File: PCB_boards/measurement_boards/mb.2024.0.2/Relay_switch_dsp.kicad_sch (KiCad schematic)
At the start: 8 parts, among them K1 G5LE-1, K2 G5LE-1, Q1 ZVN4206ASTZ, Q2 ZVN4206ASTZ

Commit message: update measurement board
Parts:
- Q1, Q2: symbol ZVN4206ASTZ:ZVN4206ASTZ -> ZVN4206A:ZVN4206ASTZ; Manufacturer_Name Diodes Incorporated -> Diodes Inc.
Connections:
- net out_12v_DPS renamed out_12v_DSP
- net out_GND_DPS renamed out_GND_DSP

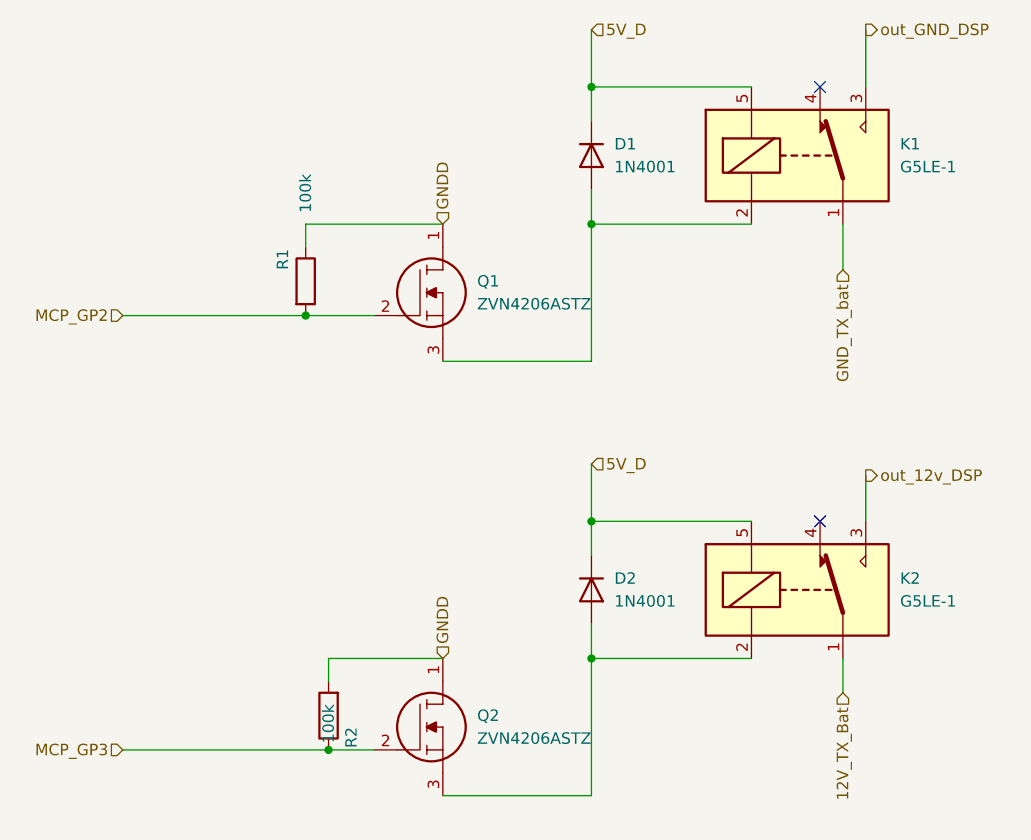
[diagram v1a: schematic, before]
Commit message: update diode 1n4007
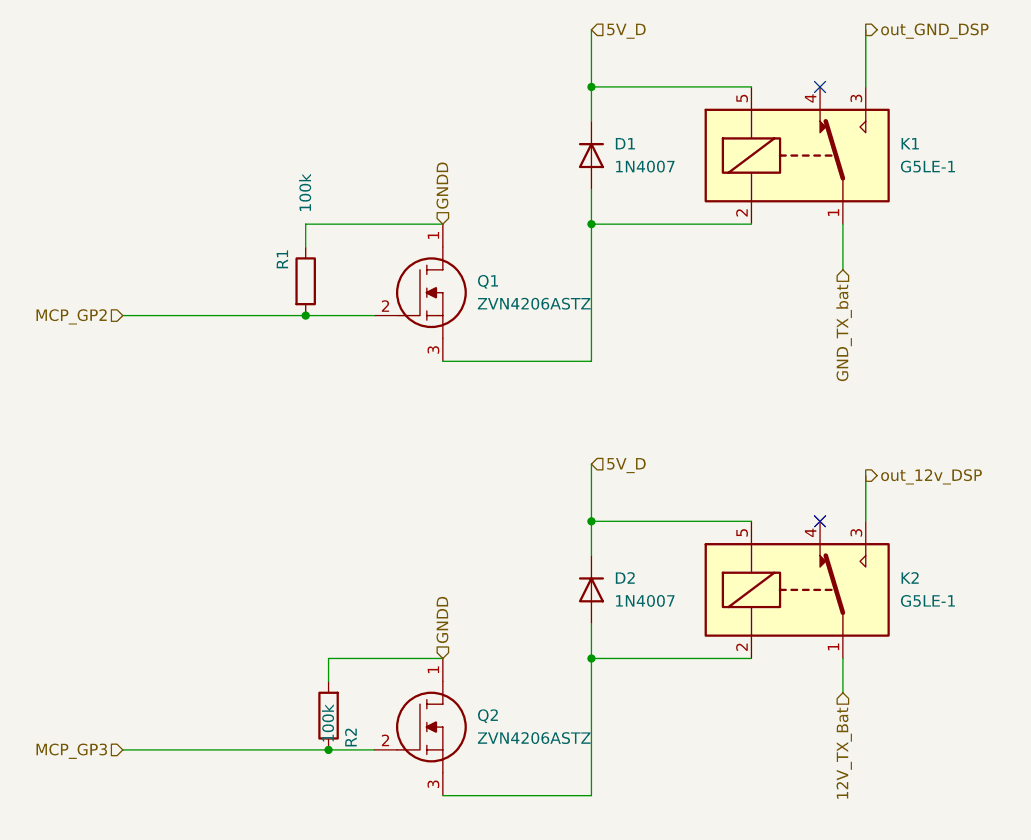
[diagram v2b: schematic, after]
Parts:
- D1, D2: value 1N4001 -> 1N4007
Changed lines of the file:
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@@
       (effects (font (size 1.27 1.27)) (justify left))
     )
-    (property "Value" "1N4001" (at 118.11 114.2999 90)
+    (property "Value" "1N4007" (at 118.11 114.2999 90)
       (effects (font (size 1.27 1.27)) (justify left))
     )
@@
       (effects (font (size 1.27 1.27)) (justify left))
     )
-    (property "Value" "1N4001" (at 118.11 66.0399 90)
+    (property "Value" "1N4007" (at 118.11 66.0399 90)
       (effects (font (size 1.27 1.27)) (justify left))
     )
